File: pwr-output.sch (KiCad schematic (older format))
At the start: 0 parts

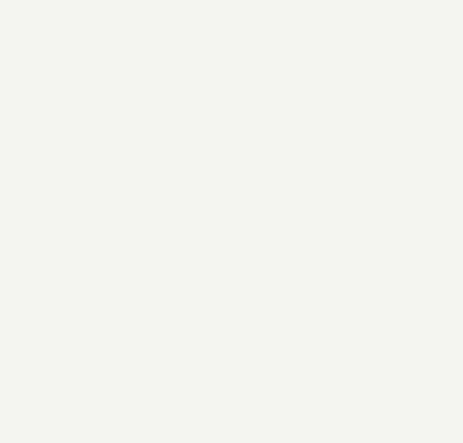
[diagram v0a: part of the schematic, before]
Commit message: Fuse on battery input
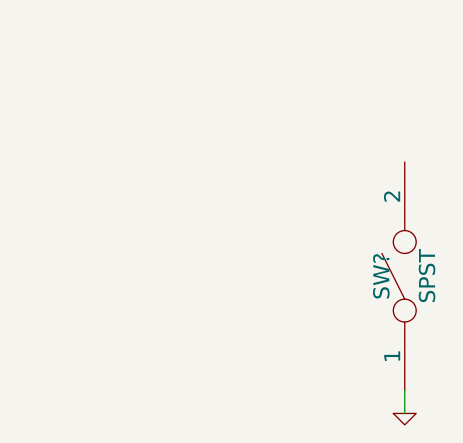
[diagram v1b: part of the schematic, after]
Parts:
- added SW?: SPST, ~, symbol SPST
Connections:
- new net GND: SW?.1
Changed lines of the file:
@@
 Sheet 3 5
 Title ""
-Date "28 dec 2014"
+Date "11 jan 2015"
 Rev ""
 Comp ""
@@
 Text HLabel 1400 2050 0    60   Input ~ 0
 PWR
+$Comp
+L SPST SW?
+U 1 1 54A6BDB2
+P 4750 3900
+F 0 "SW?" H 4750 4000 70  0000 C CNN
+F 1 "SPST" H 4750 3800 70  0000 C CNN
+F 2 "~" H 4750 3900 60  0000 C CNN
+F 3 "~" H 4750 3900 60  0000 C CNN
+	1    4750 3900
+	0    -1   -1   0
+$EndComp
+$Comp
+L GND #PWR?
+U 1 1 54A6BDC1
+P 4750 4500
+F 0 "#PWR?" H 4750 4500 30  0001 C CNN
+F 1 "GND" H 4750 4430 30  0001 C CNN
+F 2 "" H 4750 4500 60  0000 C CNN
+F 3 "" H 4750 4500 60  0000 C CNN
+	1    4750 4500
+	1    0    0    -1
+$EndComp
+Wire Wire Line
+	4750 4500 4750 4400
 $EndSCHEMATC
